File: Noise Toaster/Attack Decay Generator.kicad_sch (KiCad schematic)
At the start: 19 parts, among them Q3 2N5457, Q9 2N3906, U2 LM324

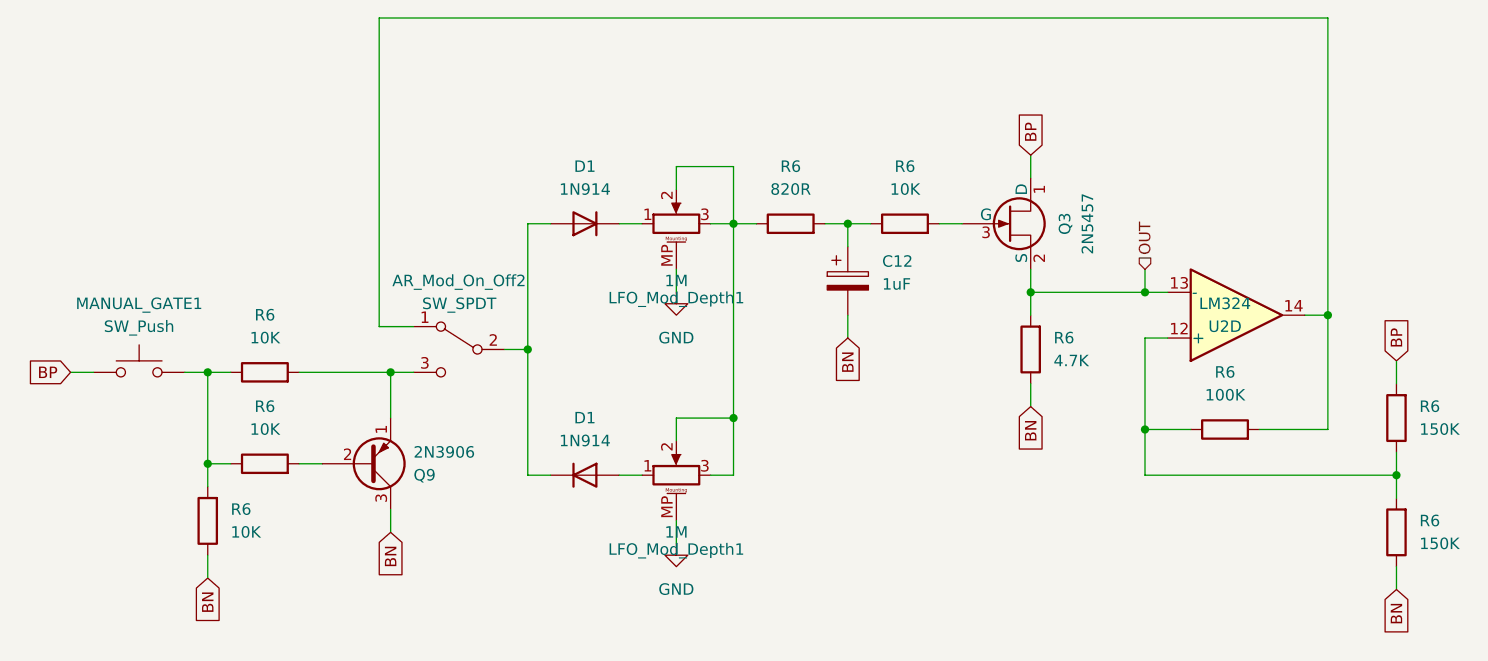
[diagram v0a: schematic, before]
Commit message: Noise Toaster - fixes after first board
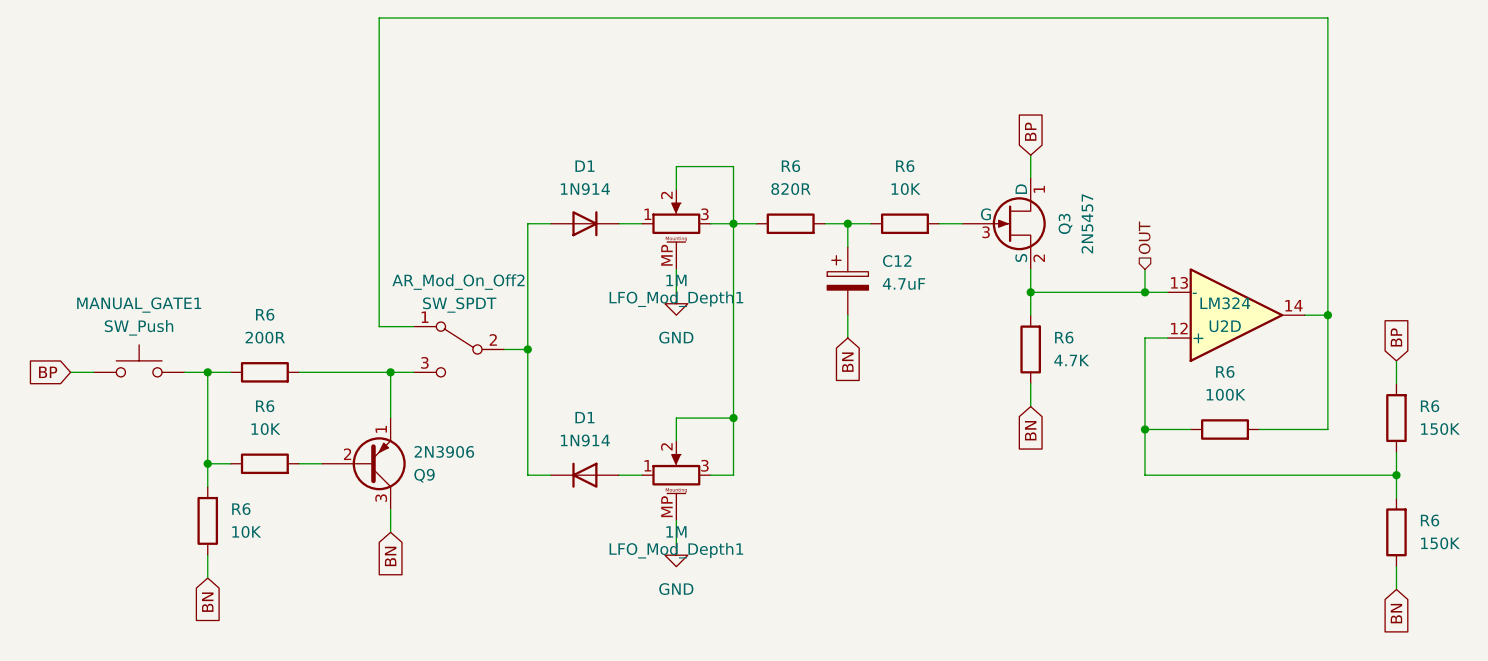
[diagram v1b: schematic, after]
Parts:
- C12: value 1uF -> 4.7uF
- R6: value 10K -> 200R
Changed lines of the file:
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@@
       (effects (font (size 1.27 1.27)))
     )
-    (property "Value" "10K" (at 92.71 106.68 90)
+    (property "Value" "200R" (at 92.71 106.68 90)
       (effects (font (size 1.27 1.27)))
     )
@@
       (effects (font (size 1.27 1.27)) (justify left))
     )
-    (property "Value" "1uF" (at 161.29 100.711 0)
+    (property "Value" "4.7uF" (at 161.29 100.711 0)
       (effects (font (size 1.27 1.27)) (justify left))
     )

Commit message: misc
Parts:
- renumbered LFO_Mod_Depth1 to ATTACK_TIME1, C12 to C21, D1 to D3, D1 to D4, AR_Mod_On_Off2 to MANUAL_REPEAT1, R6 to R49, R6 to R50, R6 to R51, R6 to R52, R6 to R53, R6 to R54, R6 to R55, R6 to R56, R6 to R57, LFO_Mod_Depth1 to RELEASE_TIME1
